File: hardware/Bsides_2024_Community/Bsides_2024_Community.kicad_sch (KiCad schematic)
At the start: 39 parts, among them J1 Conn_02x03_Odd_Even, J2 Battery, J3 Battery, J4 OLED, P1 USB_C_Plug_USB2.0, Q1 DMG3415U-7, SW1 ON, SW2 RESET, SW3 BOOT, SW4 RESET, SW6 RESET, U1 ESP32-C6-WROOM-1U-N4, U2 AP2112K-3.3

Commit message: feat(Hw): Start new floorplan
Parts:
- J2, J3: footprint bsides:BH-AAA-A1aj001 -> Community:BATT_8BH-AA-A1AJ020_MYG
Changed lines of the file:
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@@
 			)
 		)
-		(property "Footprint" "bsides:BH-AAA-A1aj001"
+		(property "Footprint" "Community:BATT_8BH-AA-A1AJ020_MYG"
 			(at 97.028 185.166 0)
 			(effects
@@
 			)
 		)
-		(property "Footprint" "bsides:BH-AAA-A1aj001"
+		(property "Footprint" "Community:BATT_8BH-AA-A1AJ020_MYG"
 			(at 97.028 179.959 0)
 			(effects

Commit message: feat(Hw): Update PCB
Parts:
- added J5, J6: Conn_01x05, Connector_PinHeader_2.54mm:PinHeader_1x05_P2.54mm_Vertical, symbol Connector_Generic:Conn_01x05
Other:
- moved on the sheet: J1, J4
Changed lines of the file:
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@@
 	(wire
 		(pts
-			(xy 95.758 133.604) (xy 102.108 133.604)
+			(xy 73.66 125.73) (xy 80.01 125.73)
 		)
 		(stroke
@@
 	(wire
 		(pts
-			(xy 95.758 131.064) (xy 102.108 131.064)
+			(xy 73.66 123.19) (xy 80.01 123.19)
 		)
 		(stroke
@@
 	(wire
 		(pts
-			(xy 95.758 128.524) (xy 102.108 128.524)
+			(xy 73.66 120.65) (xy 80.01 120.65)
 		)
 		(stroke
@@
 	(wire
 		(pts
-			(xy 95.758 125.984) (xy 102.108 125.984)
+			(xy 73.66 118.11) (xy 80.01 118.11)
 		)
 		(stroke
@@
 	)
 	(label "GND"
-		(at 95.758 128.524 0)
+		(at 73.66 120.65 0)
 		(fields_autoplaced yes)
 		(effects
@@
 	)
 	(label "SDA"
-		(at 95.758 133.604 0)
+		(at 73.66 125.73 0)
 		(fields_autoplaced yes)
 		(effects
@@
 	)
 	(label "SCL"
-		(at 95.758 131.064 0)
+		(at 73.66 123.19 0)
 		(fields_autoplaced yes)
 		(effects
@@
 	(symbol
 		(lib_id "Connector:Screw_Terminal_01x04")
-		(at 107.188 128.524 0)
+		(at 85.09 120.65 0)
 		(unit 1)
 		(exclude_from_sim no)
@@
 		(fields_autoplaced yes)
 		(property "Reference" "J4"
-			(at 109.474 128.5239 0)
+			(at 87.376 120.6499 0)
 			(effects
 				(font
@@
 		)
 		(property "Value" "OLED"
-			(at 109.474 131.0639 0)
+			(at 87.376 123.1899 0)
 			(effects
 				(font
@@
 		)
 		(property "Footprint" "bsides:Display OLED 128 x32"
-			(at 107.188 128.524 0)
+			(at 85.09 120.65 0)
 			(effects
 				(font
@@
 		)
 		(property "Datasheet" "~"
-			(at 107.188 128.524 0)
+			(at 85.09 120.65 0)
 			(effects
 				(font
@@
 		)
 		(property "Description" ""
-			(at 107.188 128.524 0)
+			(at 85.09 120.65 0)
 			(effects
 				(font
@@
 		)
 		(property "manf#" "I2C SH1106 Display Oled Azul 128×64 1.3 ” "
-			(at 107.188 128.524 0)
+			(at 85.09 120.65 0)
 			(effects
 				(font
@@
 		)
 		(property "provedor" "UNIT Electronics"
-			(at 107.188 128.524 0)
+			(at 85.09 120.65 0)
 			(effects
 				(font
@@
 	(symbol
 		(lib_id "Connector_Generic:Conn_02x03_Odd_Even")
-		(at 36.068 118.11 0)
+		(at 36.068 121.92 0)
 		(unit 1)
 		(exclude_from_sim no)
@@
 		(fields_autoplaced yes)
 		(property "Reference" "J1"
-			(at 37.338 109.728 0)
+			(at 37.338 113.538 0)
 			(effects
 				(font
@@
 		)
 		(property "Value" "Conn_02x03_Odd_Even"
-			(at 37.338 112.268 0)
+			(at 37.338 116.078 0)
 			(effects
 				(font
@@
 		)
 		(property "Footprint" "Connector_PinSocket_2.54mm:PinSocket_2x03_P2.54mm_Vertical"
-			(at 36.068 118.11 0)
+			(at 36.068 121.92 0)
 			(effects
 				(font
@@
 		)
 		(property "Datasheet" "~"
-			(at 36.068 118.11 0)
+			(at 36.068 121.92 0)
 			(effects
 				(font
@@
 		)
 		(property "Description" "Generic connector, double row, 02x03, odd/even pin numbering scheme (row 1 odd numbers, row 2 even numbers), script generated (kicad-library-utils/schlib/autogen/connector/)"
-			(at 36.068 118.11 0)
+			(at 36.068 121.92 0)
 			(effects
 				(font
@@
 	)
 	(symbol
+		(lib_id "Connector_Generic:Conn_01x05")
+		(at 146.05 121.92 0)
+		(unit 1)
+		(exclude_from_sim no)
+		(in_bom yes)
+		(on_board yes)
+		(dnp no)
+		(fields_autoplaced yes)
+		(property "Reference" "J6"
+			(at 148.59 120.6499 0)
+			(effects
+				(font
+					(size 1.27 1.27)
+				)
+				(justify left)
+			)
+		)
+		(property "Value" "Conn_01x05"
+			(at 148.59 123.1899 0)
+			(effects
+				(font
+					(size 1.27 1.27)
+				)
+				(justify left)
+			)
+		)
+		(property "Footprint" "Connector_PinHeader_2.54mm:PinHeader_1x05_P2.54mm_Vertical"
+			(at 146.05 121.92 0)
+			(effects
+				(font
+					(size 1.27 1.27)
+				)
+				(hide yes)
+			)
+		)
+		(property "Datasheet" "~"
+			(at 146.05 121.92 0)
+			(effects
+				(font
+					(size 1.27 1.27)
+				)
+				(hide yes)
+			)
+		)
+		(property "Description" "Generic connector, single row, 01x05, script generated (kicad-library-utils/schlib/autogen/connector/)"
+			(at 146.05 121.92 0)
+			(effects
+				(font
+					(size 1.27 1.27)
+				)
+				(hide yes)
+			)
+		)
+		(pin "1"
+		)
+		(pin "2"
+		)
+		(pin "4"
+		)
+		(pin "5"
+		)
+		(pin "3"
+		)
+		(instances
+			(project "Bsides_2024_Community"
+				(path "/6a5355b1-c85c-49dc-9496-6016569e49c5"
+					(reference "J6")
+					(unit 1)
+				)
+			)
+		)
+	)
+	(symbol
 		(lib_id "power:GND")
 		(at 267.589 53.34 0)
@@
 	(symbol
 		(lib_id "power:+3V3")
-		(at 95.758 125.984 0)
+		(at 73.66 118.11 0)
 		(unit 1)
 		(exclude_from_sim no)
@@
 		(dnp no)
 		(property "Reference" "#PWR012"
-			(at 95.758 129.794 0)
+			(at 73.66 121.92 0)
 			(effects
 				(font
@@
 		)
 		(property "Value" "+3V3"
-			(at 96.139 121.5898 0)
+			(at 74.041 113.7158 0)
 			(effects
 				(font
@@
 		)
 		(property "Footprint" ""
-			(at 95.758 125.984 0)
+			(at 73.66 118.11 0)
 			(effects
 				(font
@@
 		)
 		(property "Datasheet" ""
-			(at 95.758 125.984 0)
+			(at 73.66 118.11 0)
 			(effects
 				(font
@@
 		)
 		(property "Description" ""
-			(at 95.758 125.984 0)
+			(at 73.66 118.11 0)
 			(effects
 				(font
@@
 					(unit 1)
 				)
+			)
+		)
+	)
+	(symbol
+		(lib_id "Connector_Generic:Conn_01x05")
+		(at 115.57 121.92 0)
+		(unit 1)
+		(exclude_from_sim no)
+		(in_bom yes)
+		(on_board yes)
+		(dnp no)
+		(fields_autoplaced yes)
+		(property "Reference" "J5"
+			(at 118.11 120.6499 0)
+			(effects
+				(font
+					(size 1.27 1.27)
+				)
+				(justify left)
+			)
+		)
+		(property "Value" "Conn_01x05"
+			(at 118.11 123.1899 0)
+			(effects
+				(font
+					(size 1.27 1.27)
+				)
+				(justify left)
+			)
+		)
+		(property "Footprint" "Connector_PinHeader_2.54mm:PinHeader_1x05_P2.54mm_Vertical"
+			(at 115.57 121.92 0)
+			(effects
+				(font
+					(size 1.27 1.27)
+				)
+				(hide yes)
+			)
+		)
+		(property "Datasheet" "~"
+			(at 115.57 121.92 0)
+			(effects
+				(font
+					(size 1.27 1.27)
+				)
+				(hide yes)
+			)
+		)
+		(property "Description" "Generic connector, single row, 01x05, script generated (kicad-library-utils/schlib/autogen/connector/)"
+			(at 115.57 121.92 0)
+			(effects
+				(font
+					(size 1.27 1.27)
+				)
+				(hide yes)
+			)
+		)
+		(pin "1"
+		)
+		(pin "2"
+		)
+		(pin "4"
+		)
+		(pin "5"
+		)
+		(pin "3"
+		)
+		(instances
+			(project "Bsides_2024_Community"
+				(path "/6a5355b1-c85c-49dc-9496-6016569e49c5"
+					(reference "J5")
+					(unit 1)
+				)

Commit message: feat(Hw): Update PCB
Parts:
- added C13: 1uF, Capacitor_SMD:C_0603_1608Metric, symbol Device:C_Small
- added C14, C15: 10uF, Capacitor_SMD:C_0603_1608Metric, symbol Device:C_Small
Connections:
- net +3V3: now also C13.1, C14.1, C15.1
- net GND: now also C13.2, C14.2, C15.2
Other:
- moved on the sheet: C3, C4, F1, P1, R3, R4, R5, SW2, SW3

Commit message: feat(Hw): Update PCB
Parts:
- J1: value Conn_02x03_Odd_Even -> Add_On
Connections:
- net GND: now also J1.2 (Pin_2)
- net SCL: now also J1.4 (Pin_4)
- net SDA: now also J1.3 (Pin_3)
- net VBUS: now also C1.1, U2.1 (VIN), U2.3 (EN); no longer D1.2 (A), Q1.1 (G), R2.1
- net VOUT: now reaches J1.1 (Pin_1)
- net VOUT: now also C12.2, C13.1, C14.1, C15.1, C5.2, C6.2, C7.2, D2.1 (VDD), D3.1 (VDD), D4.1 (VDD), D5.1 (VDD), J4.1 (Pin_1), R1.2, R5.2, SW1.2 (B), U1.2 (3V3)
- removed net +3V3: C12.2, C13.1, C14.1, C15.1, C2.1, C5.2, C6.2, C7.2, D2.1 (VDD), D3.1 (VDD), D4.1 (VDD), D5.1 (VDD), J4.1 (Pin_1), R1.2, R5.2, U1.2 (3V3), U2.5 (VOUT)
- new net: C2.1, D1.2 (A), Q1.1 (G), R2.1, U2.5 (VOUT)
- no-connect marks 13 -> 15
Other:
- moved on the sheet: C1, C13, C14, C15, C2, C4, D1, J2, J3, Q1, R2, R5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

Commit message: feat(Hw): Update schematics
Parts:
- J4: manf# I2C SH1106 Display Oled Azul 128×64 1.3 ” -> Display OLED 128×32 0.91 I2C SSD1306 Blanco / Azul
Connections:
- net GND: now also J4.4 (Pin_4); no longer J4.2 (Pin_2)
- net SCL: now also J4.2 (Pin_2); no longer J4.3 (Pin_3)
- net SDA: now also J4.1 (Pin_1); no longer J4.4 (Pin_4)
- net VOUT: now also J4.3 (Pin_3); no longer J4.1 (Pin_1)
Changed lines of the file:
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@@
 		)
 	)
+	(wire
+		(pts
+			(xy 80.01 119.38) (xy 77.47 119.38)
+		)
+		(stroke
+			(width 0)
+			(type default)
+		)
+	)
 	(polyline
 		(pts
@@
 	(wire
 		(pts
-			(xy 73.66 125.73) (xy 80.01 125.73)
-		)
-		(stroke
-			(width 0)
-			(type default)
-		)
-	)
-	(wire
-		(pts
 			(xy 68.326 170.18) (xy 77.47 170.18)
 		)
@@
 	(wire
 		(pts
-			(xy 73.66 123.19) (xy 80.01 123.19)
-		)
-		(stroke
-			(width 0)
-			(type default)
-		)
-	)
-	(wire
-		(pts
 			(xy 90.805 168.91) (xy 90.805 170.18)
 		)
@@
 	(wire
 		(pts
+			(xy 80.01 127) (xy 77.47 127)
+		)
+		(stroke
+			(width 0)
+			(type default)
+		)
+	)
+	(wire
+		(pts
 			(xy 265.303 88.9) (xy 260.223 88.9)
 		)
@@
 	(wire
 		(pts
-			(xy 73.66 118.11) (xy 80.01 118.11)
-		)
-		(stroke
-			(width 0)
-			(type default)
-		)
-	)
-	(wire
-		(pts
 			(xy 149.479 170.053) (xy 149.479 169.037)
 		)
@@
 	(wire
 		(pts
-			(xy 73.66 120.65) (xy 80.01 120.65)
-		)
-		(stroke
-			(width 0)
-			(type default)
-		)
-	)
-	(wire
-		(pts
 			(xy 155.702 46.99) (xy 155.702 47.625)
 		)
@@
 	(wire
 		(pts
+			(xy 80.01 121.92) (xy 77.47 121.92)
+		)
+		(stroke
+			(width 0)
+			(type default)
+		)
+	)
+	(wire
+		(pts
 			(xy 100.33 46.99) (xy 100.33 49.53)
 		)
@@
 		)
 	)
+	(wire
+		(pts
+			(xy 80.01 124.46) (xy 77.47 124.46)
+		)
+		(stroke
+			(width 0)
+			(type default)
+		)
+	)
 	(text "USB-C"
 		(exclude_from_sim no)
@@
 		)
 	)
-	(label "GND"
-		(at 73.66 120.65 0)
-		(fields_autoplaced yes)
-		(effects
-			(font
-				(size 1.27 1.27)
-			)
-			(justify left bottom)
-		)
-	)
 	(label "SDA"
 		(at 31.75 120.65 0)
@@
 	)
 	(label "VOUT"
-		(at 73.66 118.11 0)
-		(fields_autoplaced yes)
-		(effects
-			(font
-				(size 1.27 1.27)
-			)
-			(justify left bottom)
-		)
-	)
-	(label "VOUT"
 		(at 100.33 46.99 180)
 		(fields_autoplaced yes)
@@
 		)
 	)
-	(label "VOUT"
-		(at 32.258 114.3 180)
+	(label "SDA"
+		(at 77.47 119.38 180)
 		(fields_autoplaced yes)
 		(effects
@@
 		)
 	)
-	(label "SDA"
-		(at 73.66 125.73 0)
+	(label "GND"
+		(at 77.47 127 180)
 		(fields_autoplaced yes)
 		(effects
@@
 				(size 1.27 1.27)
 			)
-			(justify left bottom)
+			(justify right bottom)
 		)
 	)
-	(label "GPIO22"
-		(at 250.571 65.786 180)
+	(label "VOUT"
+		(at 32.258 114.3 180)
 		(fields_autoplaced yes)
 		(effects
@@
 		)
 	)
-	(label "BOOT"
-		(at 24.892 71.12 0)
+	(label "GPIO22"
+		(at 250.571 65.786 180)
 		(fields_autoplaced yes)
 		(effects
@@
 				(size 1.27 1.27)
 			)
-			(justify left bottom)
+			(justify right bottom)
 		)
 	)
-	(label "SCL"
-		(at 73.66 123.19 0)
+	(label "BOOT"
+		(at 24.892 71.12 0)
 		(fields_autoplaced yes)
 		(effects
@@
 		)
 	)
+	(label "VOUT"
+		(at 77.47 124.46 180)
+		(fields_autoplaced yes)
+		(effects
+			(font
+				(size 1.27 1.27)
+			)
+			(justify right bottom)
+		)
+	)
 	(label "RX"
 		(at 62.738 68.326 0)
@@
 		)
 	)
+	(label "SCL"
+		(at 77.47 121.92 180)
+		(fields_autoplaced yes)
+		(effects
+			(font
+				(size 1.27 1.27)
+			)
+			(justify right bottom)
+		)
+	)
 	(label "GPIO15"
 		(at 62.738 71.12 0)
@@
 	)
 	(symbol
-		(lib_id "Connector:Screw_Terminal_01x04")
-		(at 85.09 120.65 0)
-		(unit 1)
-		(exclude_from_sim no)
-		(in_bom yes)
-		(on_board yes)
-		(dnp no)
-		(fields_autoplaced yes)
-		(property "Reference" "J4"
-			(at 87.376 120.6499 0)
-			(effects
-				(font
-					(size 1.27 1.27)
-				)
-				(justify left)
-			)
-		)
-		(property "Value" "OLED"
-			(at 87.376 123.1899 0)
-			(effects
-				(font
-					(size 1.27 1.27)
-				)
-				(justify left)
-			)
-		)
-		(property "Footprint" "bsides:Display OLED 128 x32"
-			(at 85.09 120.65 0)
-			(effects
-				(font
-					(size 1.27 1.27)
-				)
-				(hide yes)
-			)
-		)
-		(property "Datasheet" "~"
-			(at 85.09 120.65 0)
-			(effects
-				(font
-					(size 1.27 1.27)
-				)
-				(hide yes)
-			)
-		)
-		(property "Description" ""
-			(at 85.09 120.65 0)
-			(effects
-				(font
-					(size 1.27 1.27)
-				)
-				(hide yes)
-			)
-		)
-		(property "manf#" "I2C SH1106 Display Oled Azul 128×64 1.3 ” "
-			(at 85.09 120.65 0)
-			(effects
-				(font
-					(size 1.27 1.27)
-				)
-				(hide yes)
-			)
-		)
-		(property "provedor" "UNIT Electronics"
-			(at 85.09 120.65 0)
-			(effects
-				(font
-					(size 1.27 1.27)
-				)
-				(hide yes)
-			)
-		)
-		(pin "1"
-		)
-		(pin "2"
-		)
-		(pin "3"
-		)
-		(pin "4"
-		)
-		(instances
-			(project "Bsides_2024_Community"
-				(path "/6a5355b1-c85c-49dc-9496-6016569e49c5"
-					(reference "J4")
-					(unit 1)
-				)
-			)
-		)
-	)
-	(symbol
 		(lib_id "Device:R_Small")
 		(at 150.622 46.99 270)
@@
 					(unit 1)
 				)
+			)
+		)
+	)
+	(symbol
+		(lib_id "Connector:Screw_Terminal_01x04")
+		(at 85.09 121.92 0)
+		(unit 1)
+		(exclude_from_sim no)
+		(in_bom yes)
+		(on_board yes)
+		(dnp no)
+		(fields_autoplaced yes)
+		(property "Reference" "J4"
+			(at 87.376 121.9199 0)
+			(effects
+				(font
+					(size 1.27 1.27)
+				)
+				(justify left)
+			)
+		)
+		(property "Value" "OLED"
+			(at 87.376 124.4599 0)
+			(effects
+				(font
+					(size 1.27 1.27)
+				)
+				(justify left)
+			)
+		)
+		(property "Footprint" "bsides:Display OLED 128 x32"
+			(at 85.09 121.92 0)
+			(effects
+				(font
+					(size 1.27 1.27)
+				)
+				(hide yes)
+			)
+		)
+		(property "Datasheet" ""
+			(at 85.09 121.92 0)
+			(effects
+				(font
+					(size 1.27 1.27)
+				)
+				(hide yes)
+			)
+		)
+		(property "Description" ""
+			(at 85.09 121.92 0)
+			(effects
+				(font
+					(size 1.27 1.27)
+				)
+				(hide yes)
+			)
+		)
+		(property "manf#" "Display OLED 128×32 0.91 I2C SSD1306 Blanco / Azul"
+			(at 85.09 121.92 0)
+			(effects
+				(font
+					(size 1.27 1.27)
+				)
+				(hide yes)
+			)
+		)
+		(property "provedor" "UNIT Electronics"
+			(at 85.09 121.92 0)
+			(effects
+				(font
+					(size 1.27 1.27)
+				)
+				(hide yes)
+			)
+		)
+		(pin "1"
+		)
+		(pin "2"
+		)
+		(pin "3"
+		)
+		(pin "4"
+		)
+		(instances
+			(project "Bsides_2024_Community"
+				(path "/6a5355b1-c85c-49dc-9496-6016569e49c5"
+					(reference "J4")
+					(unit 1)
+				)

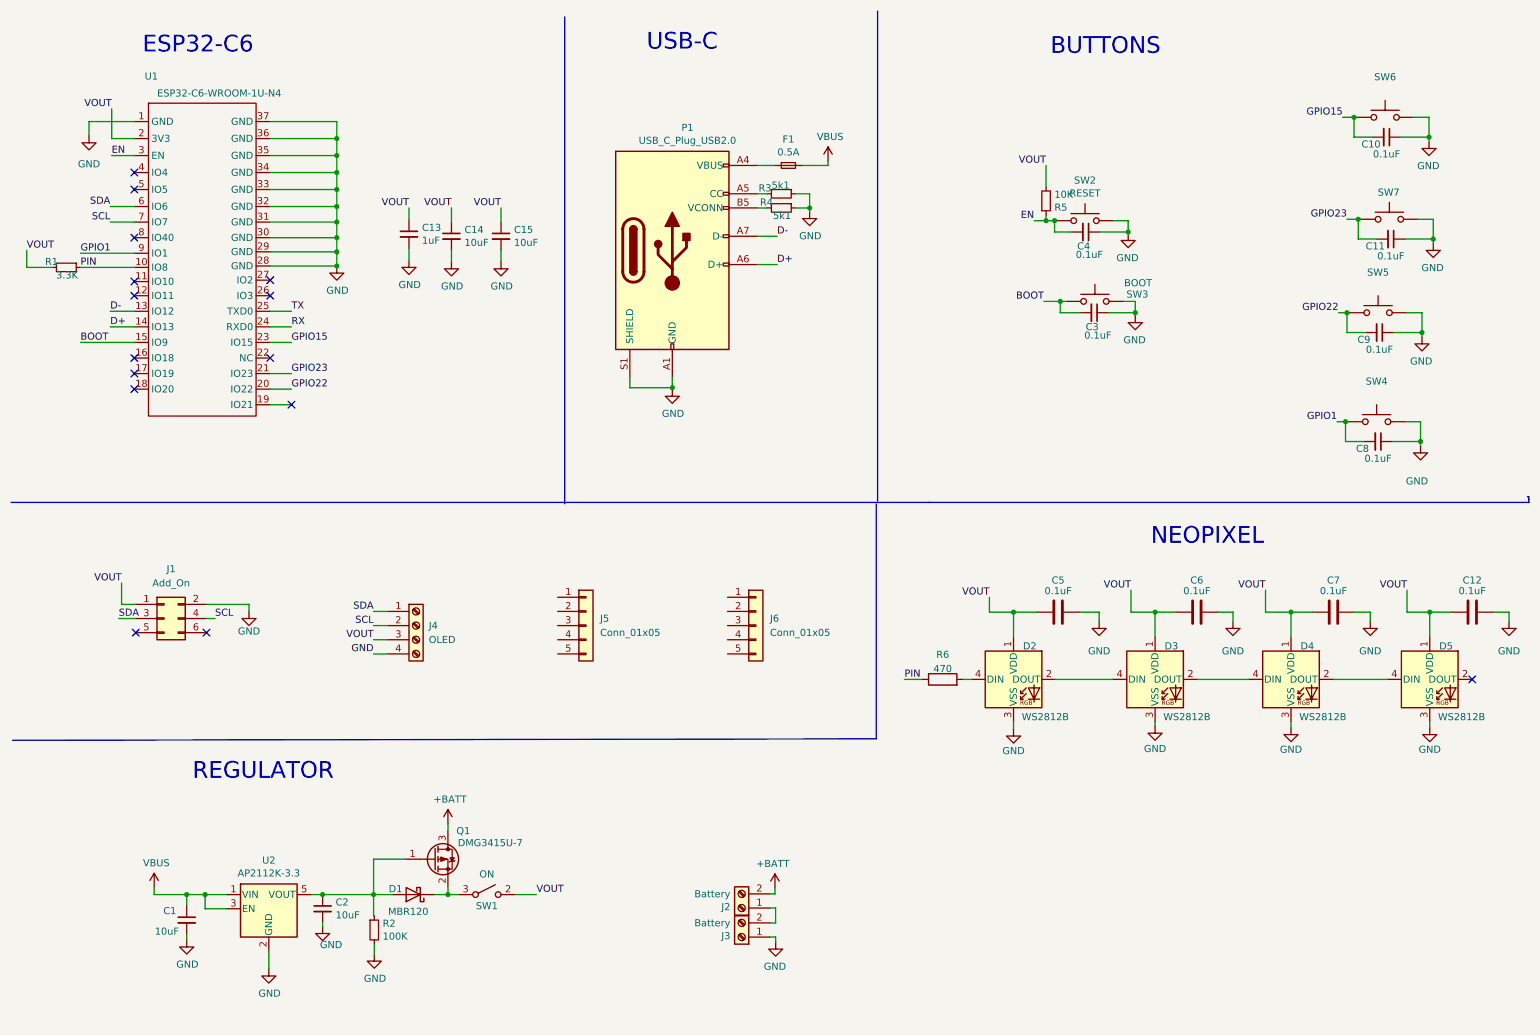
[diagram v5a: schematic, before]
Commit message: feat(Hw): Update route
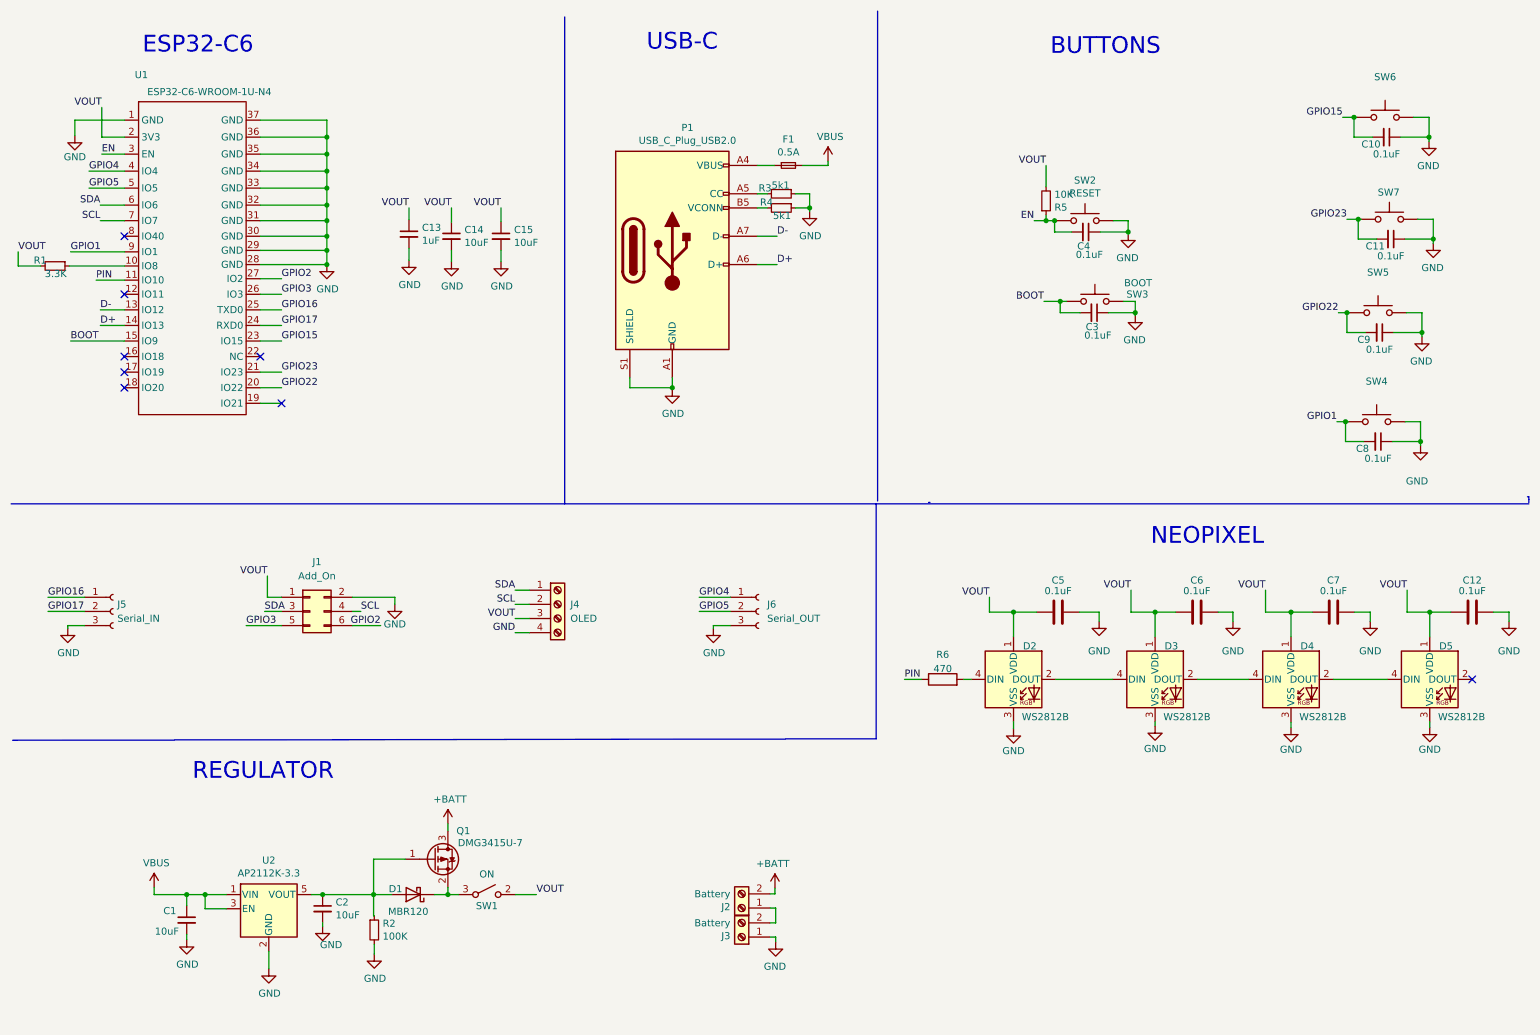
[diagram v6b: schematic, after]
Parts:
- removed J5, J6: Conn_01x05, Connector_PinHeader_2.54mm:PinHeader_1x05_P2.54mm_Vertical, symbol Connector_Generic:Conn_01x05
- added J5: Serial_IN, Connector_PinHeader_2.54mm:PinHeader_1x03_P2.54mm_Vertical, symbol Connector:Conn_01x03_Socket
- added J6: Serial_OUT, Connector_PinSocket_2.54mm:PinSocket_1x03_P2.54mm_Vertical, symbol Connector:Conn_01x03_Socket
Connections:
- net GND: now also J5.3 (Pin_3), J6.3 (Pin_3)
- net PIN: now also U1.11 (IO10); no longer R1.1, U1.10 (IO8)
- net GPIO3: now reaches J1.5 (Pin_5)
- net GPIO3: now also U1.26 (IO3)
- net GPIO2: now reaches J1.6 (Pin_6)
- net GPIO2: now also U1.27 (IO2)
- net GPIO4: now reaches U1.4 (IO4)
- net GPIO4: now also J6.1 (Pin_1)
- net GPIO5: now reaches U1.5 (IO5)
- net GPIO5: now also J6.2 (Pin_2)
- net RX renamed GPIO17
- net GPIO17: now also J5.2 (Pin_2)
- net TX renamed GPIO16
- net GPIO16: now also J5.1 (Pin_1)
- new net: R1.1, U1.10 (IO8)
- no-connect marks 15 -> 8
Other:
- moved on the sheet: J1, J4, R1, U1

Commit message: Update route and schematic
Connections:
- net GPIO1 renamed LEFT
- net GPIO15 renamed RIGHT
- net GPIO22 renamed UP
- net UP: now also SW7.2; no longer SW5.2
- net GPIO23 renamed DOWN
- net DOWN: now also SW5.2; no longer SW7.2
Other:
- moved on the sheet: C11, SW5, SW7
